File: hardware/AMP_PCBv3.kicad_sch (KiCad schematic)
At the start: 2 parts, among them CN10 Male_R2, CN7 Male_L1

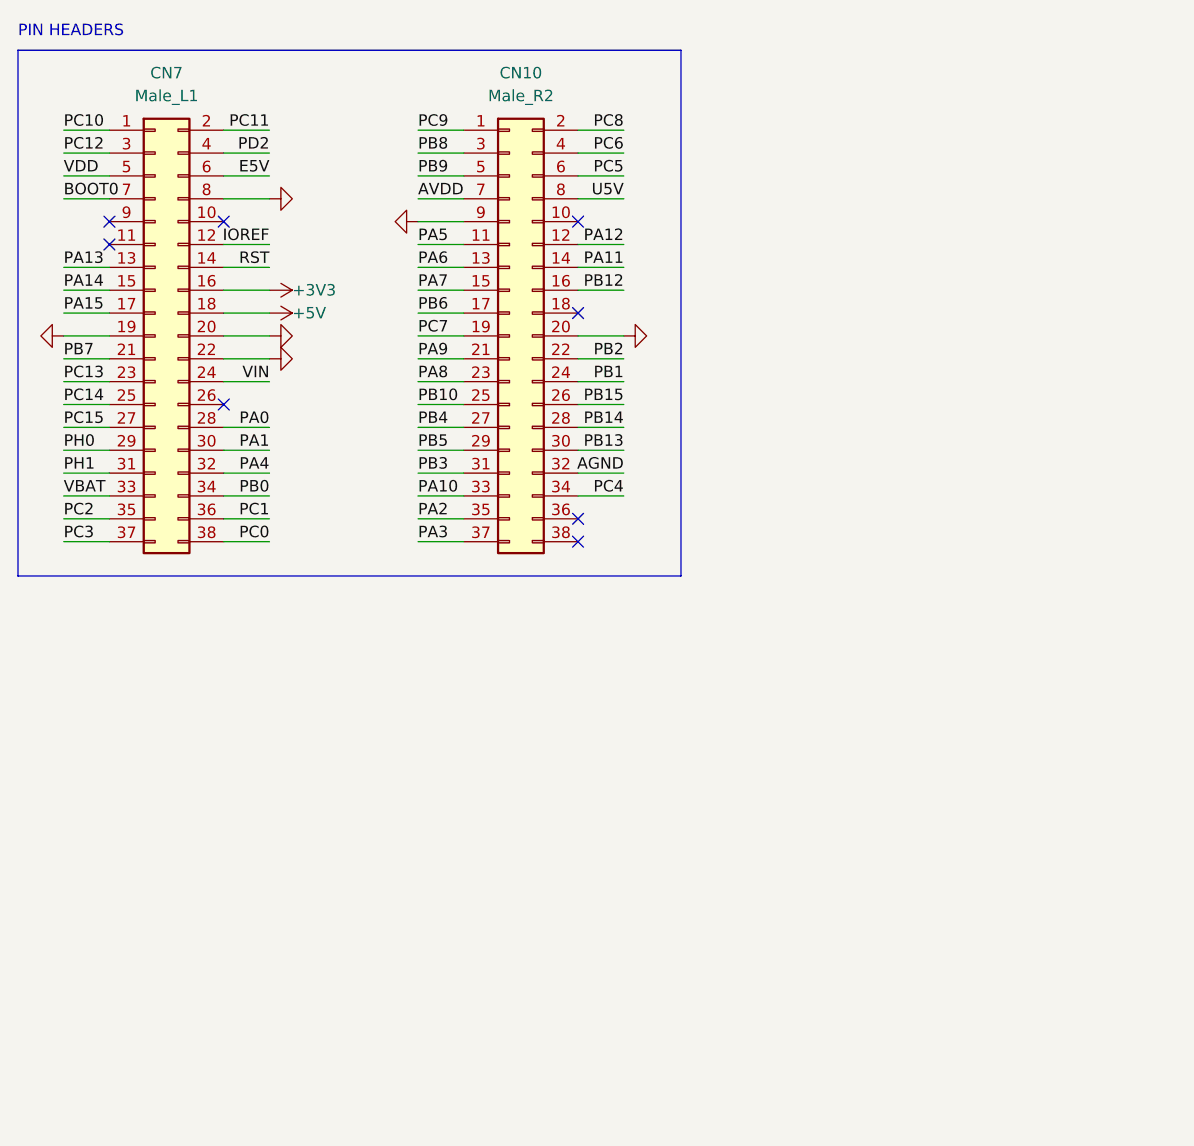
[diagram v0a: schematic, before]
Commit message: Add power circuitry and begin routing
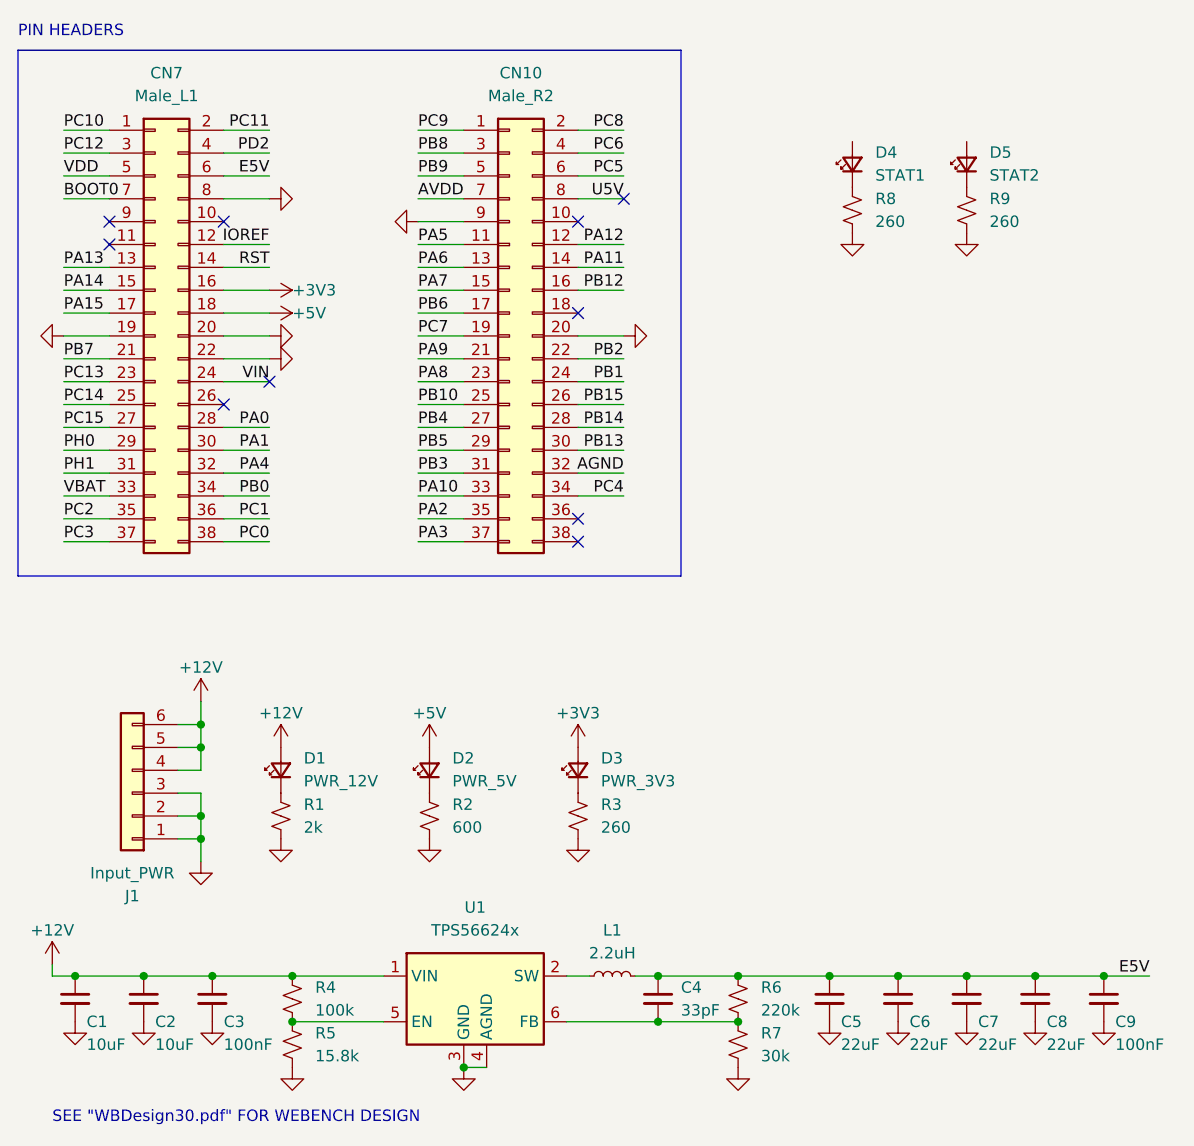
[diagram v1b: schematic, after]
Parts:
- added C1, C2: 10uF, Capacitor_SMD:C_0805_2012Metric_Pad1.18x1.45mm_HandSolder, symbol Device:C_Small
- added C3, C9: 100nF, Capacitor_SMD:C_0805_2012Metric_Pad1.18x1.45mm_HandSolder, symbol Device:C_Small
- added C4: 33pF, Capacitor_SMD:C_0805_2012Metric_Pad1.18x1.45mm_HandSolder, symbol Device:C_Small
- added C5, C6, C7, C8: 22uF, Capacitor_SMD:C_0805_2012Metric_Pad1.18x1.45mm_HandSolder, symbol Device:C_Small
- added D1: PWR_12V, LED_SMD:LED_0805_2012Metric_Pad1.15x1.40mm_HandSolder, symbol Device:LED_Small
- added D2: PWR_5V, LED_SMD:LED_0805_2012Metric_Pad1.15x1.40mm_HandSolder, symbol Device:LED_Small
- added D3: PWR_3V3, LED_SMD:LED_0805_2012Metric_Pad1.15x1.40mm_HandSolder, symbol Device:LED_Small
- added D4: STAT1, LED_SMD:LED_0805_2012Metric_Pad1.15x1.40mm_HandSolder, symbol Device:LED_Small
- added D5: STAT2, LED_SMD:LED_0805_2012Metric_Pad1.15x1.40mm_HandSolder, symbol Device:LED_Small
- added J1: Input_PWR, Connector_JST:JST_PH_B6B-PH-K_1x06_P2.00mm_Vertical, symbol Connector_Generic:Conn_01x06
- added L1: 2.2uH, Inductor_SMD:L_Vishay_IHLP-2525, symbol Device:L_Small
- added R1: 2k, Resistor_SMD:R_0805_2012Metric_Pad1.20x1.40mm_HandSolder, symbol Device:R_Small_US
- added R2: 600, Resistor_SMD:R_0805_2012Metric_Pad1.20x1.40mm_HandSolder, symbol Device:R_Small_US
- added R3, R8, R9: 260, Resistor_SMD:R_0805_2012Metric_Pad1.20x1.40mm_HandSolder, symbol Device:R_Small_US
- added R4: 100k, Resistor_SMD:R_0805_2012Metric_Pad1.20x1.40mm_HandSolder, symbol Device:R_Small_US
- added R5: 15.8k, Resistor_SMD:R_0805_2012Metric_Pad1.20x1.40mm_HandSolder, symbol Device:R_Small_US
- added R6: 220k, Resistor_SMD:R_0805_2012Metric_Pad1.20x1.40mm_HandSolder, symbol Device:R_Small_US
- added R7: 30k, Resistor_SMD:R_0805_2012Metric_Pad1.20x1.40mm_HandSolder, symbol Device:R_Small_US
- added U1: TPS56624x, Package_TO_SOT_SMD:SOT-563, symbol AMP_Custom:TPS56624x
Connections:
- net +3V3: now also D3.2 (A)
- net +5V: now also D2.2 (A)
- net E5V: now also C4.1, C5.1, C6.1, C7.1, C8.1, C9.1, L1.2, R6.1
- net GND: now also C1.2, C2.2, C3.2, C5.2, C6.2, C7.2, C8.2, C9.2, J1.1 (Pin_1), J1.2 (Pin_2), J1.3 (Pin_3), R1.2, R2.2, R3.2, R5.2, R7.2, R8.2, R9.2, U1.3 (GND), U1.4 (AGND)
- new net: D1.1 (K), R1.1
- new net: D3.1 (K), R3.1
- new net: D2.1 (K), R2.1
- new net: D5.1 (K), R9.1
- new net: C4.2, R6.2, R7.1, U1.6 (FB)
- new net: D4.1 (K), R8.1
- new net: L1.1, U1.2 (SW)
- new net: R4.2, R5.1, U1.5 (EN)
- new net +12V: C1.1, C2.1, C3.1, D1.2 (A), J1.4 (Pin_4), J1.5 (Pin_5), J1.6 (Pin_6), R4.1, U1.1 (VIN)
- no-connect marks 8 -> 10
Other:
- note added: "SEE "WBDesign30.pdf" FOR WEBENCH DESIGN"

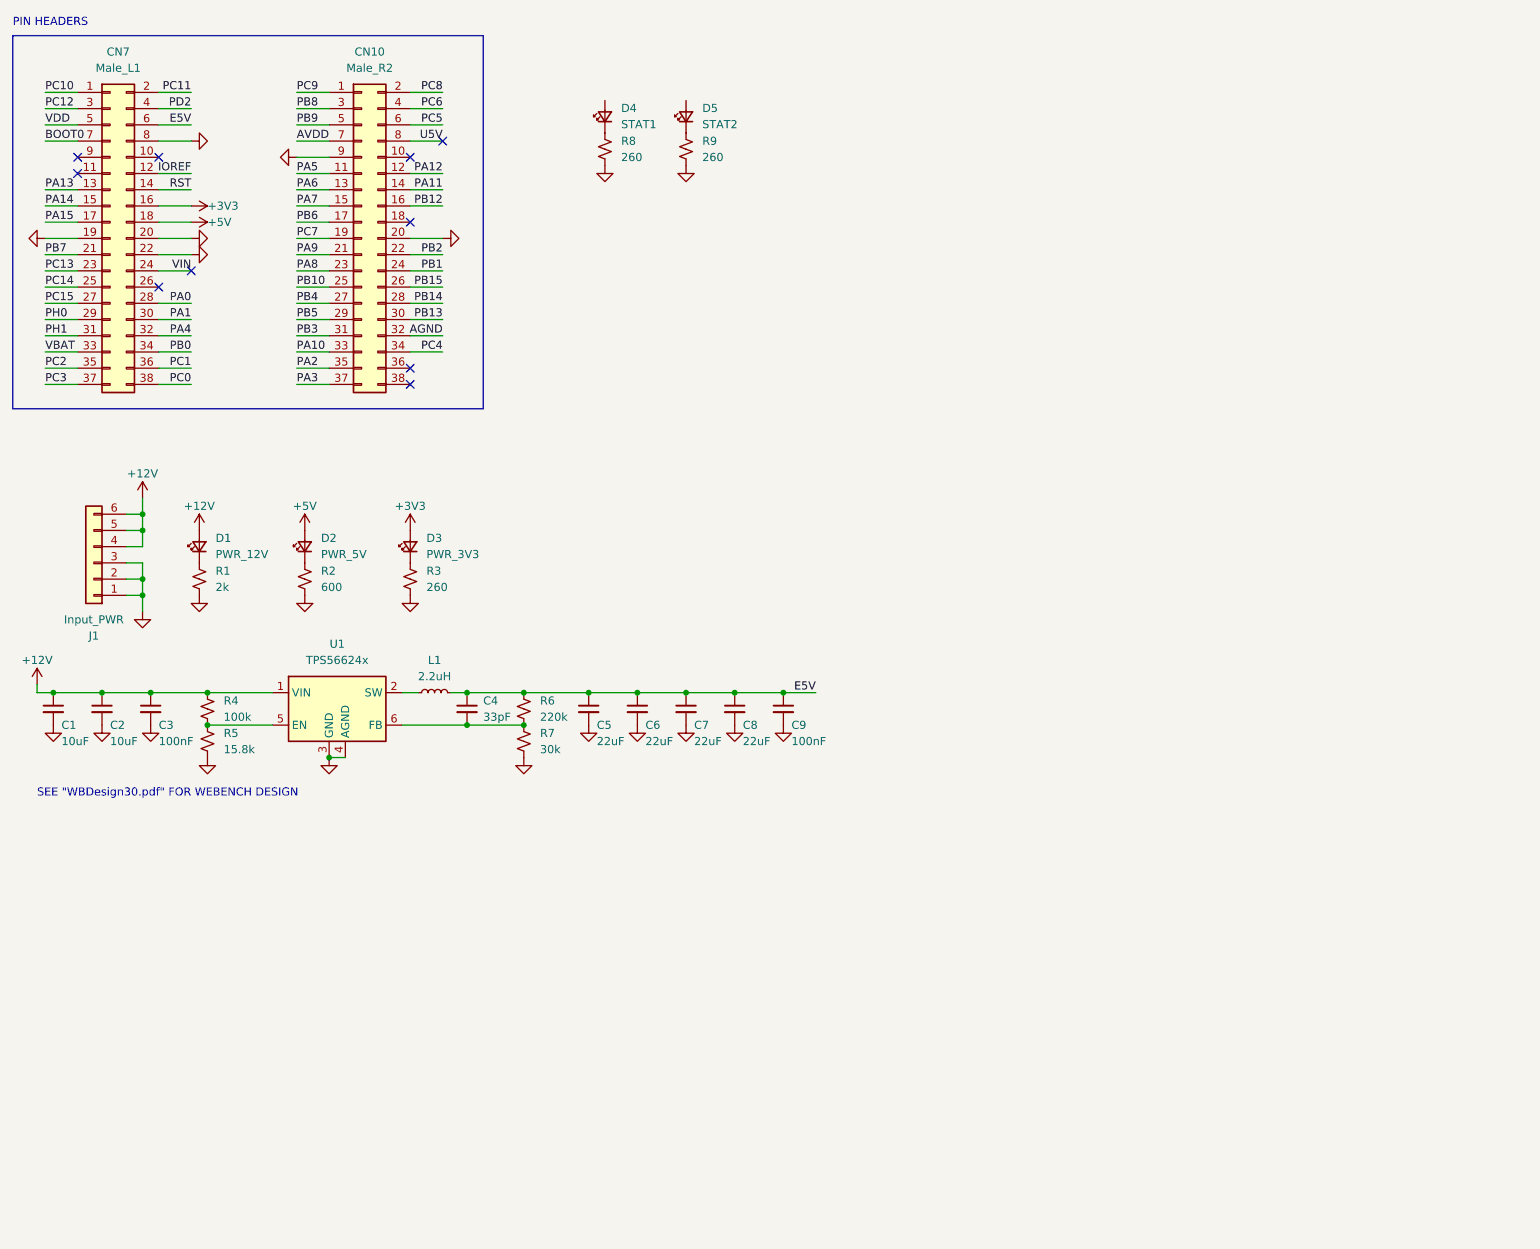
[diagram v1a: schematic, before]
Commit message: Add USB/UART and more routing
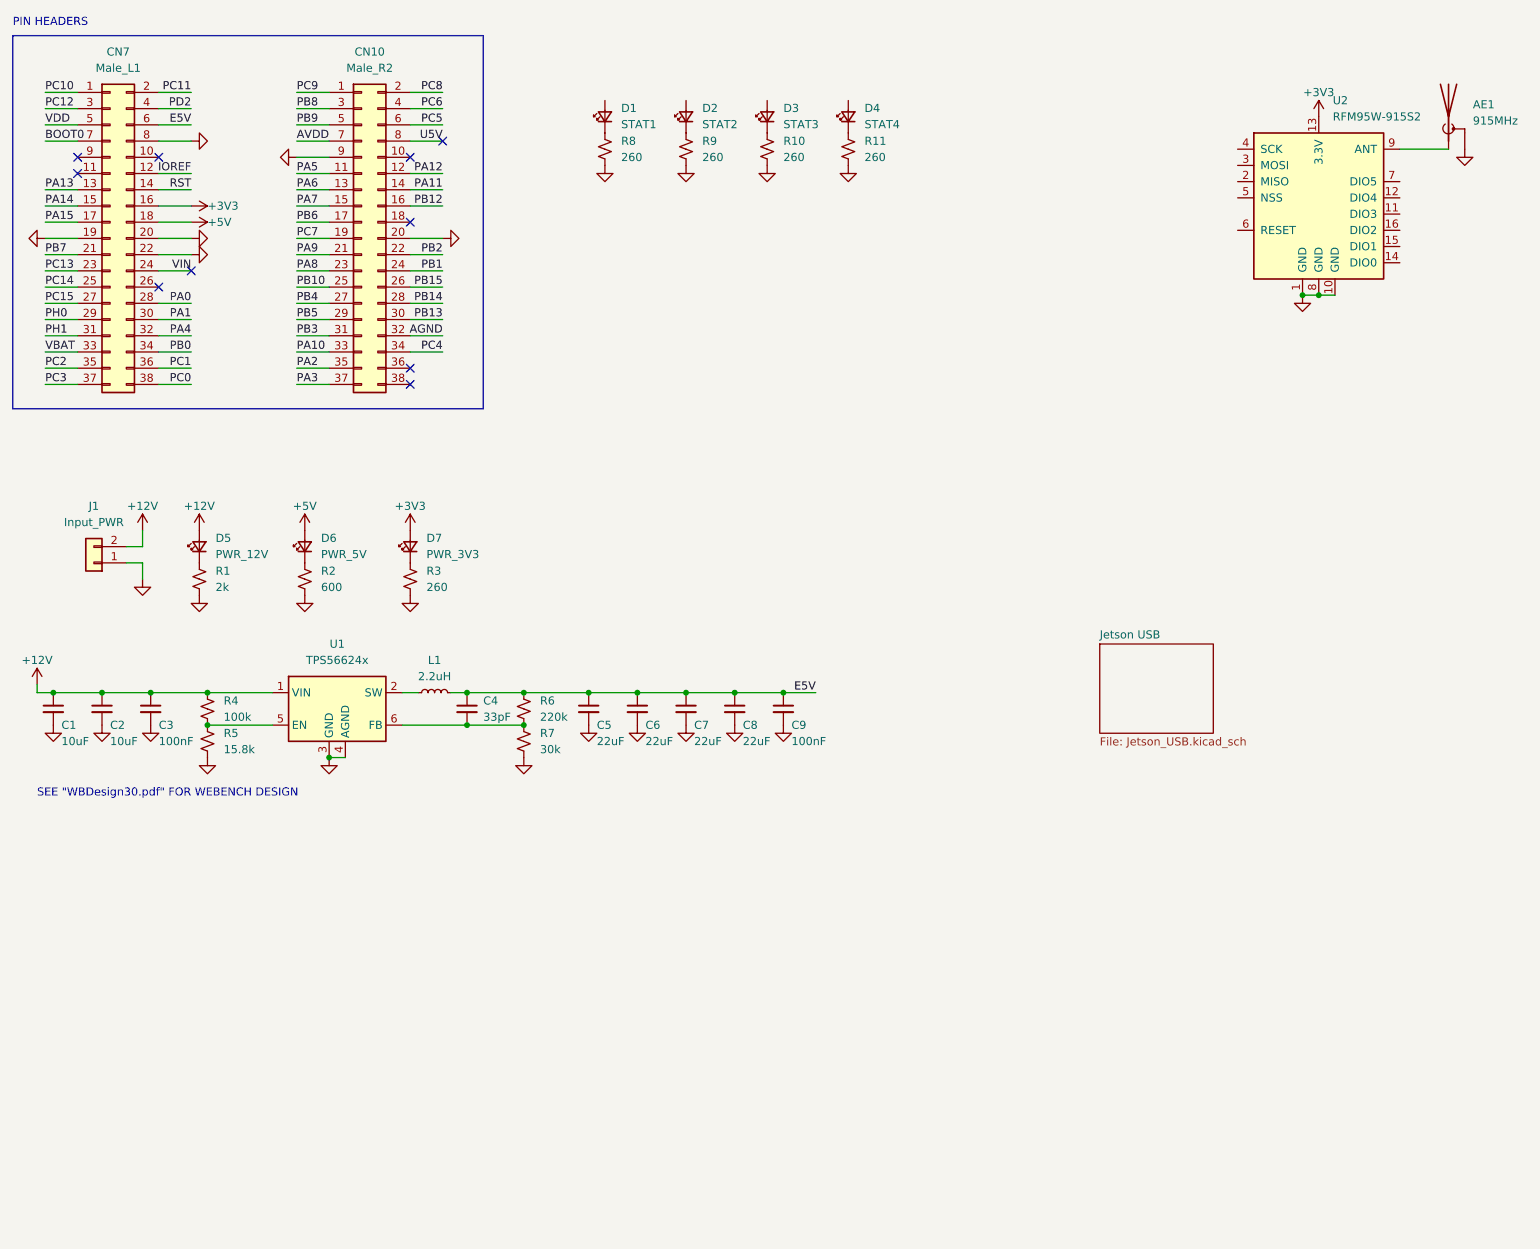
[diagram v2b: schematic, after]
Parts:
- removed J1: Input_PWR, Connector_JST:JST_PH_B6B-PH-K_1x06_P2.00mm_Vertical, symbol Connector_Generic:Conn_01x06
- added AE1: 915MHz, Connector_Coaxial:U.FL_Molex_MCRF_73412-0110_Vertical, symbol Device:Antenna_Shield
- added D3: STAT3, LED_SMD:LED_0805_2012Metric_Pad1.15x1.40mm_HandSolder, symbol Device:LED_Small
- added D4: STAT4, LED_SMD:LED_0805_2012Metric_Pad1.15x1.40mm_HandSolder, symbol Device:LED_Small
- added J1: Input_PWR, Connector_Molex:Molex_Mini-Fit_Jr_5566-02A_2x01_P4.20mm_Vertical, symbol Connector_Generic:Conn_01x02
- added R10, R11: 260, Resistor_SMD:R_0805_2012Metric_Pad1.20x1.40mm_HandSolder, symbol Device:R_Small_US
- added U2: RFM95W-915S2, RF_Module:HOPERF_RFM9XW_SMD, symbol RF_Module:RFM95W-915S2
- renumbered D4 to D1, D5 to D2, D1 to D5, D2 to D6, D3 to D7
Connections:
- net +12V: now also J1.2 (Pin_2)
- net +3V3: now also U2.13 (3.3V)
- net GND: now also AE1.2 (Shield), J1.1 (Pin_1), R10.2, R11.2, U2.1 (GND), U2.10 (GND), U2.8 (GND)
- new net: AE1.1 (A), U2.9 (ANT)
- new net: D3.1 (K), R10.1
- new net: D4.1 (K), R11.1
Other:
- added sheet Jetson USB (Jetson_USB.kicad_sch)

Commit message: Add new brake controller and inductor 3D model
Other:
- added sheet Brake Controller (Brake_Controller.kicad_sch)
- sheet Jetson USB ports: added RX, TX; removed none
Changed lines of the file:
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@@
+      (effects (font (size 1.27 1.27)) (justify left top))
+    )
+    (pin "TX" input (at 205.74 118.11 0)
+      (effects (font (size 1.27 1.27)) (justify right))
+    )
+    (pin "RX" input (at 205.74 120.65 0)
+      (effects (font (size 1.27 1.27)) (justify right))
+    )
+    (instances
+      (project "AMP_PCBv3"
+        (path "/b0eed686-2b97-4c99-952c-ca5393e47dfe" (page "3"))
+      )
+    )
+  )
+  (sheet (at 158.75 72.39) (size 22.86 15.24) (fields_autoplaced)
+    (stroke (width 0.1524) (type solid))
+    (fill (color 0 0 0 0.0000))
+    (property "Sheetname" "Brake Controller" (at 158.75 71.6784 0)
+      (effects (font (size 1.27 1.27)) (justify left bottom))
+    )
+    (property "Sheetfile" "Brake_Controller.kicad_sch" (at 158.75 88.2146 0)
       (effects (font (size 1.27 1.27)) (justify left top))
     )
